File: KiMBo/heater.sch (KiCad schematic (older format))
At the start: 61 parts, among them Q10 DMP3098L-7, Q11 2N7002, Q12 2N7002, Q13 DMP3098L-7, Q14 DMP3098L-7, Q5 2N7002, Q6 IPD90P03P4-04, Q7 2N7002, Q8 2N7002, Q9 DMP3098L-7

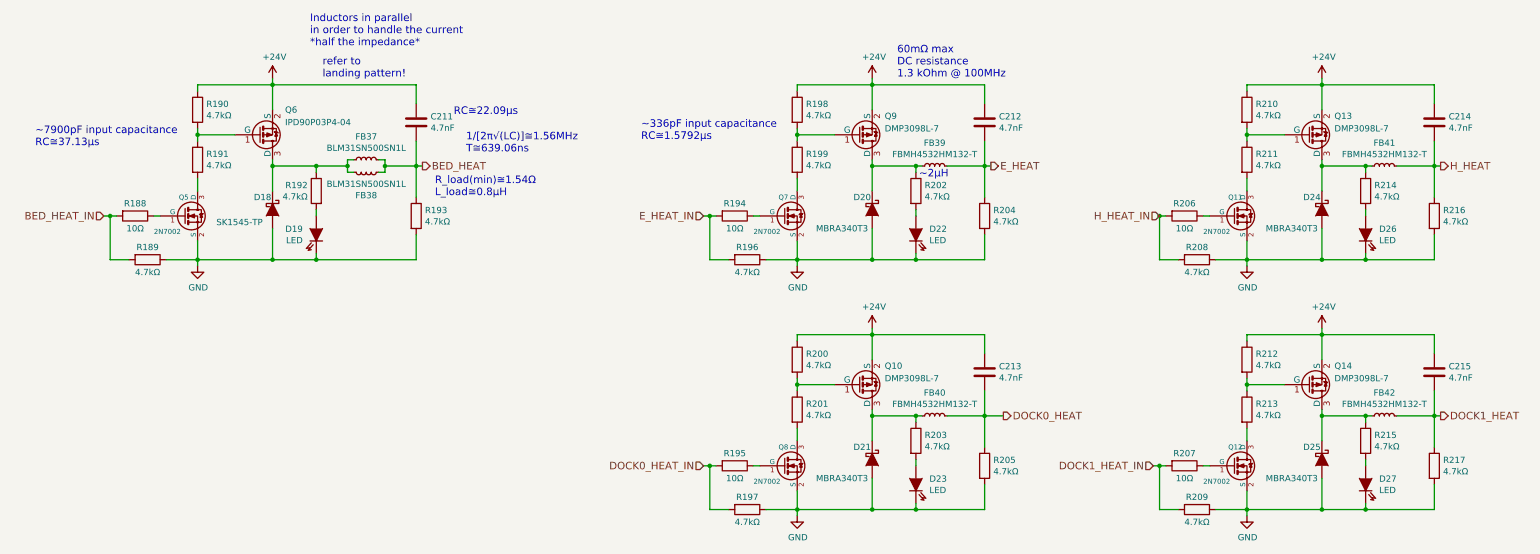
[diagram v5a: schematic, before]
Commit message: Add more footprints and more associations, one association left!
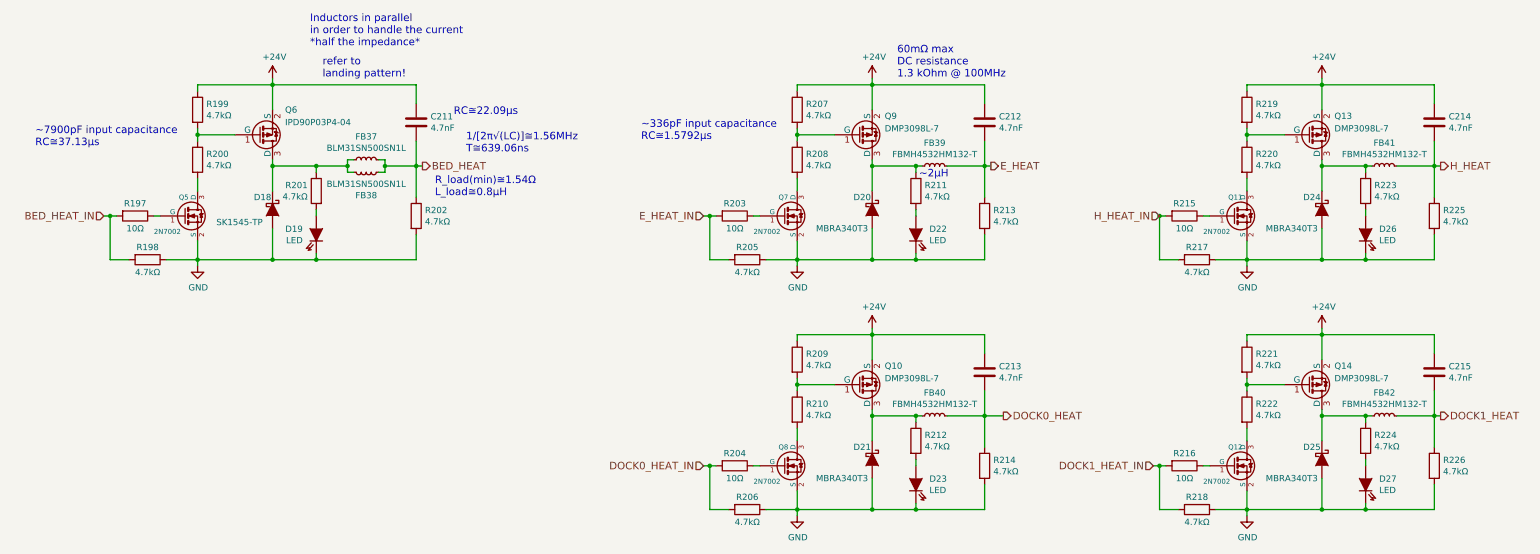
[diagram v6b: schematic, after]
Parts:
- renumbered R188 to R197, R189 to R198, R190 to R199, R191 to R200, R192 to R201, R193 to R202, R194 to R203, R195 to R204, R196 to R205, R197 to R206, R198 to R207, R199 to R208, R200 to R209, R201 to R210, R202 to R211, R203 to R212, R204 to R213, R205 to R214, R206 to R215, R207 to R216, R208 to R217, R209 to R218, R210 to R219, R211 to R220, R212 to R221, R213 to R222, R214 to R223, R215 to R224, R216 to R225, R217 to R226
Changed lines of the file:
@@
 E_HEAT_IN
 $Comp
-L +24V #PWR0263
+L +24V #PWR0265
 U 1 1 57AD0A58
 P 8350 4350
-F 0 "#PWR0263" H 8350 4200 50  0001 C CNN
+F 0 "#PWR0265" H 8350 4200 50  0001 C CNN
 F 1 "+24V" H 8365 4523 50  0000 C CNN
 F 2 "" H 8350 4350 50  0000 C CNN
@@
 $EndComp
 $Comp
-L GND #PWR0264
+L GND #PWR0266
 U 1 1 57AD222C
 P 7750 5850
-F 0 "#PWR0264" H 7750 5600 50  0001 C CNN
+F 0 "#PWR0266" H 7750 5600 50  0001 C CNN
 F 1 "GND" H 7755 5677 50  0000 C CNN
 F 2 "" H 7750 5850 50  0000 C CNN
@@
 $EndComp
 $Comp
-L R R202
+L R R211
 U 1 1 57AE0A1D
 P 8700 5250
-F 0 "R202" H 8770 5296 50  0000 L CNN
+F 0 "R211" H 8770 5296 50  0000 L CNN
 F 1 "4.7kΩ" H 8770 5205 50  0000 L CNN
 F 2 "Resistors_SMD:R_0603" V 8630 5250 50  0001 C CNN
@@
 $EndComp
 $Comp
-L GND #PWR0265
+L GND #PWR0267
 U 1 1 57AF39EC
 P 2950 5850
-F 0 "#PWR0265" H 2950 5600 50  0001 C CNN
+F 0 "#PWR0267" H 2950 5600 50  0001 C CNN
 F 1 "GND" H 2955 5677 50  0000 C CNN
 F 2 "" H 2950 5850 50  0000 C CNN
@@
 $EndComp
 $Comp
-L R R188
+L R R197
 U 1 1 57AF67D2
 P 2450 5450
-F 0 "R188" V 2350 5450 50  0000 C CNN
+F 0 "R197" V 2350 5450 50  0000 C CNN
 F 1 "10Ω" V 2550 5450 50  0000 C CNN
 F 2 "Resistors_SMD:R_0603" V 2380 5450 50  0001 C CNN
@@
 $EndComp
 $Comp
-L R R194
+L R R203
 U 1 1 57AF68A8
 P 7250 5450
-F 0 "R194" V 7150 5450 50  0000 C CNN
+F 0 "R203" V 7150 5450 50  0000 C CNN
 F 1 "10Ω" V 7350 5450 50  0000 C CNN
 F 2 "Resistors_SMD:R_0603" V 7180 5450 50  0001 C CNN
@@
 H_HEAT_IN
 $Comp
-L +24V #PWR0266
+L +24V #PWR0268
 U 1 1 57AFEA0C
 P 11950 4350
-F 0 "#PWR0266" H 11950 4200 50  0001 C CNN
+F 0 "#PWR0268" H 11950 4200 50  0001 C CNN
 F 1 "+24V" H 11965 4523 50  0000 C CNN
 F 2 "" H 11950 4350 50  0000 C CNN
@@
 $EndComp
 $Comp
-L GND #PWR0267
+L GND #PWR0269
 U 1 1 57AFEA28
 P 11350 5850
-F 0 "#PWR0267" H 11350 5600 50  0001 C CNN
+F 0 "#PWR0269" H 11350 5600 50  0001 C CNN
 F 1 "GND" H 11355 5677 50  0000 C CNN
 F 2 "" H 11350 5850 50  0000 C CNN
@@
 $EndComp
 $Comp
-L R R206
+L R R215
 U 1 1 57AFEA51
 P 10850 5450
-F 0 "R206" V 10750 5450 50  0000 C CNN
+F 0 "R215" V 10750 5450 50  0000 C CNN
 F 1 "10Ω" V 10950 5450 50  0000 C CNN
 F 2 "Resistors_SMD:R_0603" V 10780 5450 50  0001 C CNN
@@
 DOCK0_HEAT_IN
 $Comp
-L +24V #PWR0268
+L +24V #PWR0270
 U 1 1 59DB237A
 P 8350 6350
-F 0 "#PWR0268" H 8350 6200 50  0001 C CNN
+F 0 "#PWR0270" H 8350 6200 50  0001 C CNN
 F 1 "+24V" H 8365 6523 50  0000 C CNN
 F 2 "" H 8350 6350 50  0000 C CNN
@@
 $EndComp
 $Comp
-L GND #PWR0269
+L GND #PWR0271
 U 1 1 59DB2387
 P 7750 7850
-F 0 "#PWR0269" H 7750 7600 50  0001 C CNN
+F 0 "#PWR0271" H 7750 7600 50  0001 C CNN
 F 1 "GND" H 7755 7677 50  0000 C CNN
 F 2 "" H 7750 7850 50  0000 C CNN
@@
 $EndComp
 $Comp
-L R R195
+L R R204
 U 1 1 59DB23A9
 P 7250 7450
-F 0 "R195" V 7150 7450 50  0000 C CNN
+F 0 "R204" V 7150 7450 50  0000 C CNN
 F 1 "10Ω" V 7350 7450 50  0000 C CNN
 F 2 "Resistors_SMD:R_0603" V 7180 7450 50  0001 C CNN
@@
 DOCK1_HEAT_IN
 $Comp
-L +24V #PWR0270
+L +24V #PWR0272
 U 1 1 59DB23D2
 P 11950 6350
-F 0 "#PWR0270" H 11950 6200 50  0001 C CNN
+F 0 "#PWR0272" H 11950 6200 50  0001 C CNN
 F 1 "+24V" H 11965 6523 50  0000 C CNN
 F 2 "" H 11950 6350 50  0000 C CNN
@@
 $EndComp
 $Comp
-L GND #PWR0271
+L GND #PWR0273
 U 1 1 59DB23DF
 P 11350 7850
-F 0 "#PWR0271" H 11350 7600 50  0001 C CNN
+F 0 "#PWR0273" H 11350 7600 50  0001 C CNN
 F 1 "GND" H 11355 7677 50  0000 C CNN
 F 2 "" H 11350 7850 50  0000 C CNN
@@
 $EndComp
 $Comp
-L R R207
+L R R216
 U 1 1 59DB2401
 P 10850 7450
-F 0 "R207" V 10750 7450 50  0000 C CNN
+F 0 "R216" V 10750 7450 50  0000 C CNN
 F 1 "10Ω" V 10950 7450 50  0000 C CNN
 F 2 "Resistors_SMD:R_0603" V 10780 7450 50  0001 C CNN
@@
 $EndComp
 $Comp
-L +24V #PWR0272
+L +24V #PWR0274
 U 1 1 5B13B3A2
 P 3550 4350
-F 0 "#PWR0272" H 3550 4200 50  0001 C CNN
+F 0 "#PWR0274" H 3550 4200 50  0001 C CNN
 F 1 "+24V" H 3565 4523 50  0000 C CNN
 F 2 "" H 3550 4350 50  0000 C CNN
@@
 $EndComp
 $Comp
-L R R192
+L R R201
 U 1 1 5B142C62
 P 3900 5250
-F 0 "R192" H 3969 5296 50  0000 L CNN
+F 0 "R201" H 3969 5296 50  0000 L CNN
 F 1 "4.7kΩ" H 3969 5205 50  0000 L CNN
 F 2 "Resistors_SMD:R_0603" V 3830 5250 50  0001 C CNN
@@
 $EndComp
 $Comp
-L R R193
+L R R202
 U 1 1 5B1430CF
 P 4700 5450
-F 0 "R193" H 4770 5496 50  0000 L CNN
+F 0 "R202" H 4770 5496 50  0000 L CNN
 F 1 "4.7kΩ" H 4770 5405 50  0000 L CNN
 F 2 "Resistors_SMD:R_0603" V 4630 5450 50  0001 C CNN
@@
 $EndComp
 $Comp
-L R R214
+L R R223
 U 1 1 5B14334B
 P 12300 5250
-F 0 "R214" H 12370 5296 50  0000 L CNN
+F 0 "R223" H 12370 5296 50  0000 L CNN
 F 1 "4.7kΩ" H 12370 5205 50  0000 L CNN
 F 2 "Resistors_SMD:R_0603" V 12230 5250 50  0001 C CNN
@@
 $EndComp
 $Comp
-L R R215
+L R R224
 U 1 1 5B143605
 P 12300 7250
-F 0 "R215" H 12370 7296 50  0000 L CNN
+F 0 "R224" H 12370 7296 50  0000 L CNN
 F 1 "4.7kΩ" H 12370 7205 50  0000 L CNN
 F 2 "Resistors_SMD:R_0603" V 12230 7250 50  0001 C CNN
@@
 $EndComp
 $Comp
-L R R203
+L R R212
 U 1 1 5B143AC9
 P 8700 7250
-F 0 "R203" H 8770 7296 50  0000 L CNN
+F 0 "R212" H 8770 7296 50  0000 L CNN
 F 1 "4.7kΩ" H 8770 7205 50  0000 L CNN
 F 2 "Resistors_SMD:R_0603" V 8630 7250 50  0001 C CNN
@@
 RC≅22.09μs
 $Comp
-L R R190
+L R R199
 U 1 1 5B23F809
 P 2950 4600
-F 0 "R190" H 3020 4646 50  0000 L CNN
+F 0 "R199" H 3020 4646 50  0000 L CNN
 F 1 "4.7kΩ" H 3020 4555 50  0000 L CNN
 F 2 "Resistors_SMD:R_0603" V 2880 4600 50  0001 C CNN
@@
 $EndComp
 $Comp
-L R R191
+L R R200
 U 1 1 5B23F8AE
 P 2950 5000
-F 0 "R191" H 3020 5046 50  0000 L CNN
+F 0 "R200" H 3020 5046 50  0000 L CNN
 F 1 "4.7kΩ" H 3020 4955 50  0000 L CNN
 F 2 "Resistors_SMD:R_0603" V 2880 5000 50  0001 C CNN
@@
 $EndComp
 $Comp
-L R R201
+L R R210
 U 1 1 5B241076
 P 7750 7000
-F 0 "R201" H 7820 7046 50  0000 L CNN
+F 0 "R210" H 7820 7046 50  0000 L CNN
 F 1 "4.7kΩ" H 7820 6955 50  0000 L CNN
 F 2 "Resistors_SMD:R_0603" V 7680 7000 50  0001 C CNN
@@
 $EndComp
 $Comp
-L R R200
+L R R209
 U 1 1 5B241132
 P 7750 6600
-F 0 "R200" H 7820 6646 50  0000 L CNN
+F 0 "R209" H 7820 6646 50  0000 L CNN
 F 1 "4.7kΩ" H 7820 6555 50  0000 L CNN
 F 2 "Resistors_SMD:R_0603" V 7680 6600 50  0001 C CNN
@@
 $EndComp
 $Comp
-L R R211
+L R R220
 U 1 1 5B24140B
 P 11350 5000
-F 0 "R211" H 11420 5046 50  0000 L CNN
+F 0 "R220" H 11420 5046 50  0000 L CNN
 F 1 "4.7kΩ" H 11420 4955 50  0000 L CNN
 F 2 "Resistors_SMD:R_0603" V 11280 5000 50  0001 C CNN
@@
 $EndComp
 $Comp
-L R R210
+L R R219
 U 1 1 5B2414C7
 P 11350 4600
-F 0 "R210" H 11420 4646 50  0000 L CNN
+F 0 "R219" H 11420 4646 50  0000 L CNN
 F 1 "4.7kΩ" H 11420 4555 50  0000 L CNN
 F 2 "Resistors_SMD:R_0603" V 11280 4600 50  0001 C CNN
@@
 $EndComp
 $Comp
-L R R199
+L R R208
 U 1 1 5B241578
 P 7750 5000
-F 0 "R199" H 7820 5046 50  0000 L CNN
+F 0 "R208" H 7820 5046 50  0000 L CNN
 F 1 "4.7kΩ" H 7820 4955 50  0000 L CNN
 F 2 "Resistors_SMD:R_0603" V 7680 5000 50  0001 C CNN
@@
 $EndComp
 $Comp
-L R R198
+L R R207
 U 1 1 5B241632
 P 7750 4600
-F 0 "R198" H 7820 4646 50  0000 L CNN
+F 0 "R207" H 7820 4646 50  0000 L CNN
 F 1 "4.7kΩ" H 7820 4555 50  0000 L CNN
 F 2 "Resistors_SMD:R_0603" V 7680 4600 50  0001 C CNN
@@
 $EndComp
 $Comp
-L R R212
+L R R221
 U 1 1 5B242546
 P 11350 6600
-F 0 "R212" H 11420 6646 50  0000 L CNN
+F 0 "R221" H 11420 6646 50  0000 L CNN
 F 1 "4.7kΩ" H 11420 6555 50  0000 L CNN
 F 2 "Resistors_SMD:R_0603" V 11280 6600 50  0001 C CNN
@@
 $EndComp
 $Comp
-L R R213
+L R R222
 U 1 1 5B24260C
 P 11350 7000
-F 0 "R213" H 11420 7046 50  0000 L CNN
+F 0 "R222" H 11420 7046 50  0000 L CNN
 F 1 "4.7kΩ" H 11420 6955 50  0000 L CNN
 F 2 "Resistors_SMD:R_0603" V 11280 7000 50  0001 C CNN
@@
 $EndComp
 $Comp
-L R R189
+L R R198
 U 1 1 5B24C00A
 P 2550 5800
-F 0 "R189" V 2450 5800 50  0000 C CNN
+F 0 "R198" V 2450 5800 50  0000 C CNN
 F 1 "4.7kΩ" V 2650 5800 50  0000 C CNN
 F 2 "Resistors_SMD:R_0603" V 2480 5800 50  0001 C CNN
@@
 $EndComp
 $Comp
-L R R196
+L R R205
 U 1 1 5B24CAFB
 P 7350 5800
-F 0 "R196" V 7250 5800 50  0000 C CNN
+F 0 "R205" V 7250 5800 50  0000 C CNN
 F 1 "4.7kΩ" V 7450 5800 50  0000 C CNN
 F 2 "Resistors_SMD:R_0603" V 7280 5800 50  0001 C CNN
@@
 $EndComp
 $Comp
-L R R197
+L R R206
 U 1 1 5B24CBC1
 P 7350 7800
-F 0 "R197" V 7250 7800 50  0000 C CNN
+F 0 "R206" V 7250 7800 50  0000 C CNN
 F 1 "4.7kΩ" V 7450 7800 50  0000 C CNN
 F 2 "Resistors_SMD:R_0603" V 7280 7800 50  0001 C CNN
@@
 $EndComp
 $Comp
-L R R209
+L R R218
 U 1 1 5B24D548
 P 10950 7800
-F 0 "R209" V 10850 7800 50  0000 C CNN
+F 0 "R218" V 10850 7800 50  0000 C CNN
 F 1 "4.7kΩ" V 11050 7800 50  0000 C CNN
 F 2 "Resistors_SMD:R_0603" V 10880 7800 50  0001 C CNN
@@
 $EndComp
 $Comp
-L R R208
+L R R217
 U 1 1 5B24D696
 P 10950 5800
-F 0 "R208" V 10850 5800 50  0000 C CNN
+F 0 "R217" V 10850 5800 50  0000 C CNN
 F 1 "4.7kΩ" V 11050 5800 50  0000 C CNN
 F 2 "Resistors_SMD:R_0603" V 10880 5800 50  0001 C CNN
@@
 $EndComp
 $Comp
-L R R204
+L R R213
 U 1 1 5B4363E2
 P 9250 5450
-F 0 "R204" H 9320 5496 50  0000 L CNN
+F 0 "R213" H 9320 5496 50  0000 L CNN
 F 1 "4.7kΩ" H 9320 5405 50  0000 L CNN
 F 2 "Resistors_SMD:R_0603" V 9180 5450 50  0001 C CNN
@@
 $EndComp
 $Comp
-L R R216
+L R R225
 U 1 1 5B4395FD
 P 12850 5450
-F 0 "R216" H 12920 5496 50  0000 L CNN
+F 0 "R225" H 12920 5496 50  0000 L CNN
 F 1 "4.7kΩ" H 12920 5405 50  0000 L CNN
 F 2 "Resistors_SMD:R_0603" V 12780 5450 50  0001 C CNN
@@
 $EndComp
 $Comp
-L R R217
+L R R226
 U 1 1 5B43C607
 P 12850 7450
-F 0 "R217" H 12920 7496 50  0000 L CNN
+F 0 "R226" H 12920 7496 50  0000 L CNN
 F 1 "4.7kΩ" H 12920 7405 50  0000 L CNN
 F 2 "Resistors_SMD:R_0603" V 12780 7450 50  0001 C CNN
@@
 $EndComp
 $Comp
-L R R205
+L R R214
 U 1 1 5B43EB46
 P 9250 7450
-F 0 "R205" H 9320 7496 50  0000 L CNN
+F 0 "R214" H 9320 7496 50  0000 L CNN
 F 1 "4.7kΩ" H 9320 7405 50  0000 L CNN
 F 2 "Resistors_SMD:R_0603" V 9180 7450 50  0001 C CNN

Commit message: Begin layout
Arrange all connectors to get a feel for the area.
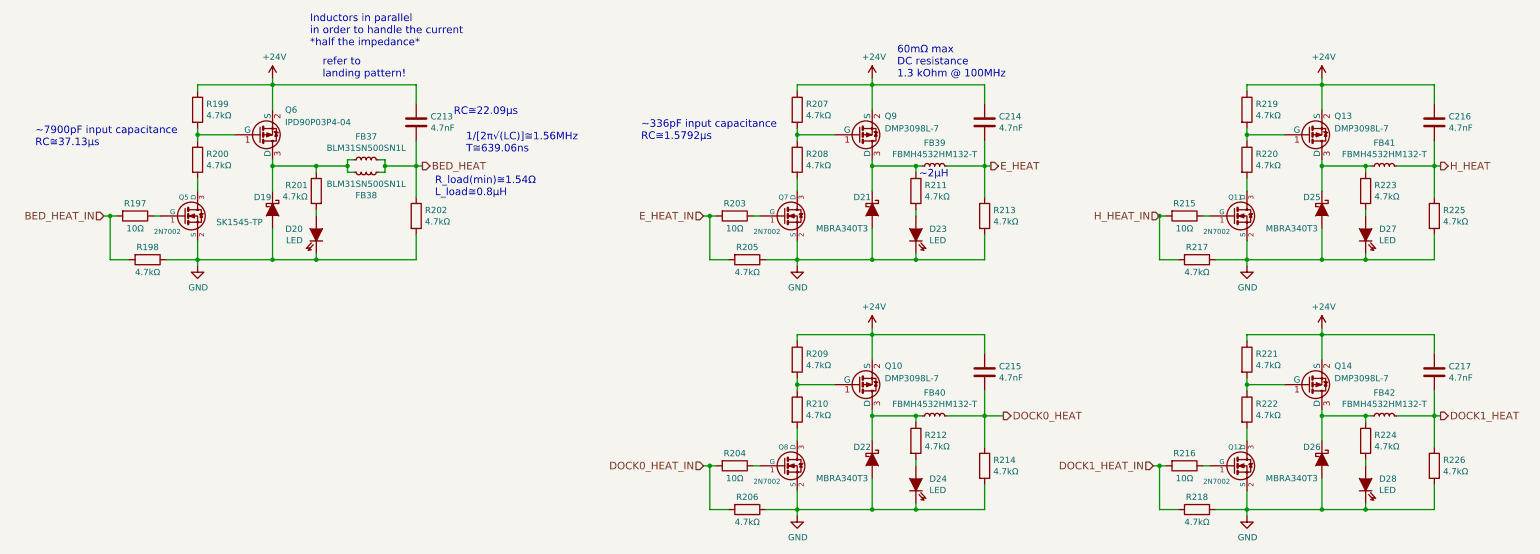
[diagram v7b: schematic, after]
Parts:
- renumbered C211 to C213, C212 to C214, C213 to C215, C214 to C216, C215 to C217, D18 to D19, D19 to D20, D20 to D21, D21 to D22, D22 to D23, D23 to D24, D24 to D25, D25 to D26, D26 to D27, D27 to D28
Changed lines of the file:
@@
 E_HEAT_IN
 $Comp
-L +24V #PWR0265
+L +24V #PWR0268
 U 1 1 57AD0A58
 P 8350 4350
-F 0 "#PWR0265" H 8350 4200 50  0001 C CNN
+F 0 "#PWR0268" H 8350 4200 50  0001 C CNN
 F 1 "+24V" H 8365 4523 50  0000 C CNN
 F 2 "" H 8350 4350 50  0000 C CNN
@@
 $EndComp
 $Comp
-L GND #PWR0266
+L GND #PWR0269
 U 1 1 57AD222C
 P 7750 5850
-F 0 "#PWR0266" H 7750 5600 50  0001 C CNN
+F 0 "#PWR0269" H 7750 5600 50  0001 C CNN
 F 1 "GND" H 7755 5677 50  0000 C CNN
 F 2 "" H 7750 5850 50  0000 C CNN
@@
 $EndComp
 $Comp
-L D_Schottky D20
+L D_Schottky D21
 U 1 1 57AE0DBA
 P 8350 5400
-F 0 "D20" V 8250 5250 50  0000 L CNN
+F 0 "D21" V 8250 5250 50  0000 L CNN
 F 1 "MBRA340T3" V 8500 4950 50  0000 L CNN
 F 2 "KiMBo:MBR-DO-214AC" H 8350 5400 50  0001 C CNN
@@
 $EndComp
 $Comp
-L GND #PWR0267
+L GND #PWR0270
 U 1 1 57AF39EC
 P 2950 5850
-F 0 "#PWR0267" H 2950 5600 50  0001 C CNN
+F 0 "#PWR0270" H 2950 5600 50  0001 C CNN
 F 1 "GND" H 2955 5677 50  0000 C CNN
 F 2 "" H 2950 5850 50  0000 C CNN
@@
 $EndComp
 $Comp
-L D_Schottky D18
+L D_Schottky D19
 U 1 1 57AF3A03
 P 3550 5400
-F 0 "D18" V 3450 5250 50  0000 L CNN
+F 0 "D19" V 3450 5250 50  0000 L CNN
 F 1 "SK1545-TP" V 3650 4950 50  0000 L CNN
 F 2 "KiMBo:SK-DO-214AB" H 3550 5400 50  0001 C CNN
@@
 H_HEAT_IN
 $Comp
-L +24V #PWR0268
+L +24V #PWR0271
 U 1 1 57AFEA0C
 P 11950 4350
-F 0 "#PWR0268" H 11950 4200 50  0001 C CNN
+F 0 "#PWR0271" H 11950 4200 50  0001 C CNN
 F 1 "+24V" H 11965 4523 50  0000 C CNN
 F 2 "" H 11950 4350 50  0000 C CNN
@@
 $EndComp
 $Comp
-L GND #PWR0269
+L GND #PWR0272
 U 1 1 57AFEA28
 P 11350 5850
-F 0 "#PWR0269" H 11350 5600 50  0001 C CNN
+F 0 "#PWR0272" H 11350 5600 50  0001 C CNN
 F 1 "GND" H 11355 5677 50  0000 C CNN
 F 2 "" H 11350 5850 50  0000 C CNN
@@
 $EndComp
 $Comp
-L D_Schottky D24
+L D_Schottky D25
 U 1 1 57AFEA3C
 P 11950 5400
-F 0 "D24" V 11850 5250 50  0000 L CNN
+F 0 "D25" V 11850 5250 50  0000 L CNN
 F 1 "MBRA340T3" V 12100 4950 50  0000 L CNN
 F 2 "KiMBo:MBR-DO-214AC" H 11950 5400 50  0001 C CNN
@@
 H_HEAT
 $Comp
-L LED_Short D19
+L LED_Short D20
 U 1 1 59526A10
 P 3900 5600
-F 0 "D19" V 3946 5492 50  0000 R CNN
+F 0 "D20" V 3946 5492 50  0000 R CNN
 F 1 "LED" V 3855 5492 50  0000 R CNN
 F 2 "LEDs:LED_0603" H 3900 5600 50  0001 C CNN
@@
 $EndComp
 $Comp
-L LED_Short D22
+L LED_Short D23
 U 1 1 59526BFD
 P 8700 5600
-F 0 "D22" V 8746 5492 50  0000 R CNN
+F 0 "D23" V 8746 5492 50  0000 R CNN
 F 1 "LED" V 8655 5492 50  0000 R CNN
 F 2 "LEDs:LED_0603" H 8700 5600 50  0001 C CNN
@@
 $EndComp
 $Comp
-L LED_Short D26
+L LED_Short D27
 U 1 1 59526F25
 P 12300 5600
-F 0 "D26" V 12346 5492 50  0000 R CNN
+F 0 "D27" V 12346 5492 50  0000 R CNN
 F 1 "LED" V 12255 5492 50  0000 R CNN
 F 2 "LEDs:LED_0603" H 12300 5600 50  0001 C CNN
@@
 DOCK0_HEAT_IN
 $Comp
-L +24V #PWR0270
+L +24V #PWR0273
 U 1 1 59DB237A
 P 8350 6350
-F 0 "#PWR0270" H 8350 6200 50  0001 C CNN
+F 0 "#PWR0273" H 8350 6200 50  0001 C CNN
 F 1 "+24V" H 8365 6523 50  0000 C CNN
 F 2 "" H 8350 6350 50  0000 C CNN
@@
 $EndComp
 $Comp
-L GND #PWR0271
+L GND #PWR0274
 U 1 1 59DB2387
 P 7750 7850
-F 0 "#PWR0271" H 7750 7600 50  0001 C CNN
+F 0 "#PWR0274" H 7750 7600 50  0001 C CNN
 F 1 "GND" H 7755 7677 50  0000 C CNN
 F 2 "" H 7750 7850 50  0000 C CNN
@@
 $EndComp
 $Comp
-L D_Schottky D21
+L D_Schottky D22
 U 1 1 59DB2394
 P 8350 7400
-F 0 "D21" V 8250 7250 50  0000 L CNN
+F 0 "D22" V 8250 7250 50  0000 L CNN
 F 1 "MBRA340T3" V 8500 6950 50  0000 L CNN
 F 2 "KiMBo:MBR-DO-214AC" H 8350 7400 50  0001 C CNN
@@
 DOCK1_HEAT_IN
 $Comp
-L +24V #PWR0272
+L +24V #PWR0275
 U 1 1 59DB23D2
 P 11950 6350
-F 0 "#PWR0272" H 11950 6200 50  0001 C CNN
+F 0 "#PWR0275" H 11950 6200 50  0001 C CNN
 F 1 "+24V" H 11965 6523 50  0000 C CNN
 F 2 "" H 11950 6350 50  0000 C CNN
@@
 $EndComp
 $Comp
-L GND #PWR0273
+L GND #PWR0276
 U 1 1 59DB23DF
 P 11350 7850
-F 0 "#PWR0273" H 11350 7600 50  0001 C CNN
+F 0 "#PWR0276" H 11350 7600 50  0001 C CNN
 F 1 "GND" H 11355 7677 50  0000 C CNN
 F 2 "" H 11350 7850 50  0000 C CNN
@@
 $EndComp
 $Comp
-L D_Schottky D25
+L D_Schottky D26
 U 1 1 59DB23EC
 P 11950 7400
-F 0 "D25" V 11850 7250 50  0000 L CNN
+F 0 "D26" V 11850 7250 50  0000 L CNN
 F 1 "MBRA340T3" V 12100 6950 50  0000 L CNN
 F 2 "KiMBo:MBR-DO-214AC" H 11950 7400 50  0001 C CNN
@@
 DOCK1_HEAT
 $Comp
-L LED_Short D23
+L LED_Short D24
 U 1 1 59DB2439
 P 8700 7600
-F 0 "D23" V 8746 7492 50  0000 R CNN
+F 0 "D24" V 8746 7492 50  0000 R CNN
 F 1 "LED" V 8655 7492 50  0000 R CNN
 F 2 "LEDs:LED_0603" H 8700 7600 50  0001 C CNN
@@
 $EndComp
 $Comp
-L LED_Short D27
+L LED_Short D28
 U 1 1 59DB2440
 P 12300 7600
-F 0 "D27" V 12346 7492 50  0000 R CNN
+F 0 "D28" V 12346 7492 50  0000 R CNN
 F 1 "LED" V 12255 7492 50  0000 R CNN
 F 2 "LEDs:LED_0603" H 12300 7600 50  0001 C CNN
@@
 $EndComp
 $Comp
-L +24V #PWR0274
+L +24V #PWR0277
 U 1 1 5B13B3A2
 P 3550 4350
-F 0 "#PWR0274" H 3550 4200 50  0001 C CNN
+F 0 "#PWR0277" H 3550 4200 50  0001 C CNN
 F 1 "+24V" H 3565 4523 50  0000 C CNN
 F 2 "" H 3550 4350 50  0000 C CNN
@@
 $EndComp
 $Comp
-L C C211
+L C C213
 U 1 1 5B142985
 P 4700 4700
-F 0 "C211" H 4815 4746 50  0000 L CNN
+F 0 "C213" H 4815 4746 50  0000 L CNN
 F 1 "4.7nF" H 4815 4655 50  0000 L CNN
 F 2 "Capacitors_SMD:C_0603" H 4738 4550 50  0001 C CNN
@@
 $EndComp
 $Comp
-L C C212
+L C C214
 U 1 1 5B4362FC
 P 9250 4700
-F 0 "C212" H 9365 4746 50  0000 L CNN
+F 0 "C214" H 9365 4746 50  0000 L CNN
 F 1 "4.7nF" H 9365 4655 50  0000 L CNN
 F 2 "Capacitors_SMD:C_0603" H 9288 4550 50  0001 C CNN
@@
 $EndComp
 $Comp
-L C C214
+L C C216
 U 1 1 5B4399C9
 P 12850 4700
-F 0 "C214" H 12965 4746 50  0000 L CNN
+F 0 "C216" H 12965 4746 50  0000 L CNN
 F 1 "4.7nF" H 12965 4655 50  0000 L CNN
 F 2 "Capacitors_SMD:C_0603" H 12888 4550 50  0001 C CNN
@@
 $EndComp
 $Comp
-L C C215
+L C C217
 U 1 1 5B43C8B7
 P 12850 6700
-F 0 "C215" H 12965 6746 50  0000 L CNN
+F 0 "C217" H 12965 6746 50  0000 L CNN
 F 1 "4.7nF" H 12965 6655 50  0000 L CNN
 F 2 "Capacitors_SMD:C_0603" H 12888 6550 50  0001 C CNN
@@
 $EndComp
 $Comp
-L C C213
+L C C215
 U 1 1 5B43EF5C
 P 9250 6700
-F 0 "C213" H 9365 6746 50  0000 L CNN
+F 0 "C215" H 9365 6746 50  0000 L CNN
 F 1 "4.7nF" H 9365 6655 50  0000 L CNN
 F 2 "Capacitors_SMD:C_0603" H 9288 6550 50  0001 C CNN
